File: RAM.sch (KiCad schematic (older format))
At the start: 13 parts, among them J9 RAM_CURRENT, U1 ATXMEGA128A1U-AU, U2 SN74AHC573PW, U3 IDT71V256SA

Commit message: Finished?
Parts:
- removed C28: 100n, IPC7351-Nominal:CAPC1005X55, symbol C-0402
- removed C4: 4u7, IPC7351-Nominal:CAPC1608X55, symbol C-0603
- removed J9: RAM_CURRENT, conn-100mil:CONN-100MIL-M-1x2, symbol CONN-100MIL-M-1x2
- removed R15: 0R1, IPC7351-Nominal:RESC1608X50, symbol R-0603
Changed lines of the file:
@@
 P 7100 5050
 AR Path="/56EF5511" Ref="#PWR?"  Part="1"
-AR Path="/56EF4451/56EF5511" Ref="#PWR?"  Part="1"
-F 0 "#PWR?" H 7100 5050 30  0001 C CNN
+AR Path="/56EF4451/56EF5511" Ref="#PWR21"  Part="1"
+F 0 "#PWR21" H 7100 5050 30  0001 C CNN
 F 1 "GND" H 7100 4980 30  0001 C CNN
 F 2 "" H 7100 5050 60  0000 C CNN
 F 3 "" H 7100 5050 60  0000 C CNN
 	1    7100 5050
-	1    0    0    -1
-$EndComp
-$Comp
-L C-0603 C?
-U 1 1 56EF5518
-P 7000 5700
-AR Path="/56EF5518" Ref="C?"  Part="1"
-AR Path="/56EF4451/56EF5518" Ref="C4"  Part="1"
-F 0 "C4" H 7113 5746 50  0000 L CNN
-F 1 "4u7" H 7113 5655 50  0000 L CNN
-F 2 "IPC7351-Nominal:CAPC1608X55" H 7000 5700 50  0001 C CNN
-F 3 "" H 6990 5675 60  0000 C CNN
-F 4 "CAP MLCC 4u7 10V ≥X5R 20% [0603]" H 7800 6250 60  0001 C CNN "BOM"
-	1    7000 5700
-	1    0    0    -1
-$EndComp
-$Comp
-L GND #PWR?
-U 1 1 56EF551F
-P 7000 5850
-AR Path="/56EF551F" Ref="#PWR?"  Part="1"
-AR Path="/56EF4451/56EF551F" Ref="#PWR?"  Part="1"
-F 0 "#PWR?" H 7000 5850 30  0001 C CNN
-F 1 "GND" H 7000 5780 30  0001 C CNN
-F 2 "" H 7000 5850 60  0000 C CNN
-F 3 "" H 7000 5850 60  0000 C CNN
-	1    7000 5850
-	1    0    0    -1
-$EndComp
-$Comp
-L C-0402 C?
-U 1 1 56EF5526
-P 7400 5700
-AR Path="/56EF5526" Ref="C?"  Part="1"
-AR Path="/56EF4451/56EF5526" Ref="C28"  Part="1"
-F 0 "C28" H 7513 5746 50  0000 L CNN
-F 1 "100n" H 7513 5655 50  0000 L CNN
-F 2 "IPC7351-Nominal:CAPC1005X55" H 7400 5700 50  0001 C CNN
-F 3 "" H 7390 5675 60  0000 C CNN
-F 4 "CAP MLCC 100n ≥X5R 10V 20% [0402]" H 8200 6250 60  0001 C CNN "BOM"
-	1    7400 5700
-	1    0    0    -1
-$EndComp
-$Comp
-L GND #PWR?
-U 1 1 56EF552D
-P 7400 5850
-AR Path="/56EF552D" Ref="#PWR?"  Part="1"
-AR Path="/56EF4451/56EF552D" Ref="#PWR?"  Part="1"
-F 0 "#PWR?" H 7400 5850 30  0001 C CNN
-F 1 "GND" H 7400 5780 30  0001 C CNN
-F 2 "" H 7400 5850 60  0000 C CNN
-F 3 "" H 7400 5850 60  0000 C CNN
-	1    7400 5850
 	1    0    0    -1
 $EndComp
@@
 P 5000 3000
 AR Path="/56EF553D" Ref="#PWR?"  Part="1"
-AR Path="/56EF4451/56EF553D" Ref="#PWR?"  Part="1"
-F 0 "#PWR?" H 5000 3000 30  0001 C CNN
+AR Path="/56EF4451/56EF553D" Ref="#PWR20"  Part="1"
+F 0 "#PWR20" H 5000 3000 30  0001 C CNN
 F 1 "GND" H 5000 2930 30  0001 C CNN
 F 2 "" H 5000 3000 60  0000 C CNN
@@
 	7100 5000 7050 5000
 Wire Wire Line
-	7000 5500 7000 5600
-Wire Wire Line
-	7000 5850 7000 5800
-Wire Wire Line
-	7400 4900 7400 5600
-Wire Wire Line
-	7400 5850 7400 5800
-Wire Wire Line
 	6050 3200 5750 3200
 Wire Wire Line
@@
 Wire Wire Line
 	3050 4700 3100 4700
-Wire Wire Line
-	6650 5500 7400 5500
-$Comp
-L +3.3 #PWR?
-U 1 1 56EF5658
-P 6250 5500
-AR Path="/56EF5658" Ref="#PWR?"  Part="1"
-AR Path="/56EF4451/56EF5658" Ref="#PWR?"  Part="1"
-F 0 "#PWR?" H 6250 5550 30  0001 C CNN
-F 1 "+3.3" V 6250 5588 50  0000 L CNN
-F 2 "" H 6250 5500 60  0000 C CNN
-F 3 "" H 6250 5500 60  0000 C CNN
-	1    6250 5500
-	0    -1   -1   0
-$EndComp
-$Comp
-L R-0603 R?
-U 1 1 56EF565F
-P 6550 5500
-AR Path="/56EF565F" Ref="R?"  Part="1"
-AR Path="/56EF4451/56EF565F" Ref="R15"  Part="1"
-F 0 "R15" V 6350 5500 50  0000 C CNN
-F 1 "0R1" V 6441 5500 50  0000 C CNN
-F 2 "IPC7351-Nominal:RESC1608X50" H 6550 5500 50  0001 C CNN
-F 3 "" H 6550 5550 60  0000 C CNN
-F 4 "RES SMD 0R1 1% [0603]" H 7300 6050 60  0001 C CNN "BOM"
-	1    6550 5500
-	0    1    1    0
-$EndComp
-Wire Wire Line
-	6250 5500 6450 5500
-$Comp
-L CONN-100MIL-M-1x2 J?
-U 1 1 56EF5668
-P 6600 5700
-AR Path="/56EF5668" Ref="J?"  Part="1"
-AR Path="/56EF4451/56EF5668" Ref="J9"  Part="1"
-F 0 "J9" V 6764 5647 50  0000 C CNN
-F 1 "RAM_CURRENT" V 6855 5647 50  0000 C CNN
-F 2 "conn-100mil:CONN-100MIL-M-1x2" H 6600 5700 50  0001 C CNN
-F 3 "" H 6600 5700 50  0000 C CNN
-F 4 "DIST DIGIKEY 3M9447-ND" H 6600 5700 60  0001 C CNN "BOM"
-	1    6600 5700
-	0    1    1    0
-$EndComp
-Wire Wire Line
-	6500 5650 6500 5600
-Wire Wire Line
-	6500 5600 6400 5600
-Wire Wire Line
-	6400 5600 6400 5500
-Connection ~ 6400 5500
-Wire Wire Line
-	6600 5650 6600 5600
-Wire Wire Line
-	6600 5600 6700 5600
-Wire Wire Line
-	6700 5600 6700 5500
-Connection ~ 6700 5500
-Text GLabel 6900 5200 2    50   Output ~ 0
+Text GLabel 7400 4900 2    50   Input ~ 0
 3V3RAM
-Wire Wire Line
-	6900 5200 6800 5200
-Wire Wire Line
-	6800 5200 6800 5500
-Connection ~ 6800 5500
-Connection ~ 7000 5500
-Connection ~ 7400 5500
 $Comp
 L TESTPOINT TP?
@@
 P 3700 3350
 AR Path="/56EF5685" Ref="#PWR?"  Part="1"
-AR Path="/56EF4451/56EF5685" Ref="#PWR?"  Part="1"
-F 0 "#PWR?" H 3700 3350 30  0001 C CNN
+AR Path="/56EF4451/56EF5685" Ref="#PWR19"  Part="1"
+F 0 "#PWR19" H 3700 3350 30  0001 C CNN
 F 1 "GND" H 3700 3280 30  0001 C CNN
 F 2 "" H 3700 3350 60  0000 C CNN

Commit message: Reannotate
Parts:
- renumbered R9 to R10, R23 to R11, R25 to R12, R26 to R13, R24 to R14, U2 to U4, U3 to U5
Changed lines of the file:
@@
 $EndDescr
 $Comp
-L IDT71V256SA U3
+L IDT71V256SA U5
 U 1 1 56EF54EE
 P 6550 4100
-F 0 "U3" H 6550 5267 50  0000 C CNN
+F 0 "U5" H 6550 5267 50  0000 C CNN
 F 1 "IDT71V256SA" H 6550 5176 50  0000 C CNN
 F 2 "IPC7351-Nominal:SOJ127P1118X375-28" H 6550 2900 60  0001 C CNN
@@
 P 5400 3200
 AR Path="/56EF5535" Ref="U?"  Part="1"
-AR Path="/56EF4451/56EF5535" Ref="U2"  Part="1"
-F 0 "U2" H 5400 3767 50  0000 C CNN
+AR Path="/56EF4451/56EF5535" Ref="U4"  Part="1"
+F 0 "U4" H 5400 3767 50  0000 C CNN
 F 1 "SN74AHC573PW" H 5400 3676 50  0000 C CNN
 F 2 "IPC7351-Nominal:SOP65P640X110-20" H 5400 1900 50  0001 C CNN
@@
 P 3200 1800
 AR Path="/56EF555B" Ref="R?"  Part="1"
-AR Path="/56EF4451/56EF555B" Ref="R9"  Part="1"
-F 0 "R9" V 3150 1550 50  0000 C CNN
+AR Path="/56EF4451/56EF555B" Ref="R10"  Part="1"
+F 0 "R10" V 3150 1550 50  0000 C CNN
 F 1 "68" V 3091 1800 50  0000 C CNN
 F 2 "IPC7351-Nominal:RESCAXE80P160X320X70-8" H 3200 1800 50  0001 C CNN
@@
 P 3200 1900
 AR Path="/56EF5563" Ref="R?"  Part="2"
-AR Path="/56EF4451/56EF5563" Ref="R9"  Part="2"
-F 0 "R9" V 3150 1650 50  0000 C CNN
+AR Path="/56EF4451/56EF5563" Ref="R10"  Part="2"
+F 0 "R10" V 3150 1650 50  0000 C CNN
 F 1 "68" V 3091 1900 50  0001 C CNN
 F 2 "IPC7351-Nominal:RESCAXE80P160X320X70-8" H 3200 1900 50  0001 C CNN
@@
 P 3200 2000
 AR Path="/56EF556B" Ref="R?"  Part="3"
-AR Path="/56EF4451/56EF556B" Ref="R9"  Part="3"
-F 0 "R9" V 3150 1750 50  0000 C CNN
+AR Path="/56EF4451/56EF556B" Ref="R10"  Part="3"
+F 0 "R10" V 3150 1750 50  0000 C CNN
 F 1 "68" V 3091 2000 50  0001 C CNN
 F 2 "IPC7351-Nominal:RESCAXE80P160X320X70-8" H 3200 2000 50  0001 C CNN
@@
 P 3200 2100
 AR Path="/56EF5573" Ref="R?"  Part="4"
-AR Path="/56EF4451/56EF5573" Ref="R9"  Part="4"
-F 0 "R9" V 3150 1850 50  0000 C CNN
+AR Path="/56EF4451/56EF5573" Ref="R10"  Part="4"
+F 0 "R10" V 3150 1850 50  0000 C CNN
 F 1 "68" V 3091 2100 50  0001 C CNN
 F 2 "IPC7351-Nominal:RESCAXE80P160X320X70-8" H 3200 2100 50  0001 C CNN
@@
 P 3200 2200
 AR Path="/56EF557B" Ref="R?"  Part="1"
-AR Path="/56EF4451/56EF557B" Ref="R23"  Part="1"
-F 0 "R23" V 3150 1950 50  0000 C CNN
+AR Path="/56EF4451/56EF557B" Ref="R11"  Part="1"
+F 0 "R11" V 3150 1950 50  0000 C CNN
 F 1 "68" V 3091 2200 50  0001 C CNN
 F 2 "IPC7351-Nominal:RESCAXE80P160X320X70-8" H 3200 2200 50  0001 C CNN
@@
 P 3200 2300
 AR Path="/56EF5583" Ref="R?"  Part="2"
-AR Path="/56EF4451/56EF5583" Ref="R23"  Part="2"
-F 0 "R23" V 3150 2050 50  0000 C CNN
+AR Path="/56EF4451/56EF5583" Ref="R11"  Part="2"
+F 0 "R11" V 3150 2050 50  0000 C CNN
 F 1 "68" V 3091 2300 50  0001 C CNN
 F 2 "IPC7351-Nominal:RESCAXE80P160X320X70-8" H 3200 2300 50  0001 C CNN
@@
 P 3200 2400
 AR Path="/56EF558B" Ref="R?"  Part="3"
-AR Path="/56EF4451/56EF558B" Ref="R23"  Part="3"
-F 0 "R23" V 3150 2150 50  0000 C CNN
+AR Path="/56EF4451/56EF558B" Ref="R11"  Part="3"
+F 0 "R11" V 3150 2150 50  0000 C CNN
 F 1 "68" V 3091 2400 50  0001 C CNN
 F 2 "IPC7351-Nominal:RESCAXE80P160X320X70-8" H 3200 2400 50  0001 C CNN
@@
 P 3200 2500
 AR Path="/56EF5593" Ref="R?"  Part="4"
-AR Path="/56EF4451/56EF5593" Ref="R23"  Part="4"
-F 0 "R23" V 3150 2250 50  0000 C CNN
+AR Path="/56EF4451/56EF5593" Ref="R11"  Part="4"
+F 0 "R11" V 3150 2250 50  0000 C CNN
 F 1 "68" V 3091 2500 50  0001 C CNN
 F 2 "IPC7351-Nominal:RESCAXE80P160X320X70-8" H 3200 2500 50  0001 C CNN
@@
 P 3200 5400
 AR Path="/56EF559B" Ref="R?"  Part="1"
-AR Path="/56EF4451/56EF559B" Ref="R24"  Part="1"
-F 0 "R24" V 3150 5150 50  0000 C CNN
+AR Path="/56EF4451/56EF559B" Ref="R14"  Part="1"
+F 0 "R14" V 3150 5150 50  0000 C CNN
 F 1 "68" V 3091 5400 50  0000 C CNN
 F 2 "IPC7351-Nominal:RESCAXE80P160X320X70-8" H 3200 5400 50  0001 C CNN
@@
 P 3200 5500
 AR Path="/56EF55A3" Ref="R?"  Part="2"
-AR Path="/56EF4451/56EF55A3" Ref="R24"  Part="2"
-F 0 "R24" V 3150 5250 50  0000 C CNN
+AR Path="/56EF4451/56EF55A3" Ref="R14"  Part="2"
+F 0 "R14" V 3150 5250 50  0000 C CNN
 F 1 "68" V 3091 5500 50  0001 C CNN
 F 2 "IPC7351-Nominal:RESCAXE80P160X320X70-8" H 3200 5500 50  0001 C CNN
@@
 P 3200 5600
 AR Path="/56EF55AB" Ref="R?"  Part="3"
-AR Path="/56EF4451/56EF55AB" Ref="R24"  Part="3"
-F 0 "R24" V 3150 5350 50  0000 C CNN
+AR Path="/56EF4451/56EF55AB" Ref="R14"  Part="3"
+F 0 "R14" V 3150 5350 50  0000 C CNN
 F 1 "68" V 3091 5600 50  0001 C CNN
 F 2 "IPC7351-Nominal:RESCAXE80P160X320X70-8" H 3200 5600 50  0001 C CNN
@@
 P 3200 5800
 AR Path="/56EF55B3" Ref="R?"  Part="4"
-AR Path="/56EF4451/56EF55B3" Ref="R24"  Part="4"
-F 0 "R24" V 3150 5550 50  0000 C CNN
+AR Path="/56EF4451/56EF55B3" Ref="R14"  Part="4"
+F 0 "R14" V 3150 5550 50  0000 C CNN
 F 1 "68" V 3091 5800 50  0001 C CNN
 F 2 "IPC7351-Nominal:RESCAXE80P160X320X70-8" H 3200 5800 50  0001 C CNN
@@
 P 3200 4000
 AR Path="/56EF55BB" Ref="R?"  Part="1"
-AR Path="/56EF4451/56EF55BB" Ref="R25"  Part="1"
-F 0 "R25" V 3150 3750 50  0000 C CNN
+AR Path="/56EF4451/56EF55BB" Ref="R12"  Part="1"
+F 0 "R12" V 3150 3750 50  0000 C CNN
 F 1 "68" V 3091 4000 50  0000 C CNN
 F 2 "IPC7351-Nominal:RESCAXE80P160X320X70-8" H 3200 4000 50  0001 C CNN
@@
 P 3200 4100
 AR Path="/56EF55C3" Ref="R?"  Part="2"
-AR Path="/56EF4451/56EF55C3" Ref="R25"  Part="2"
-F 0 "R25" V 3150 3850 50  0000 C CNN
+AR Path="/56EF4451/56EF55C3" Ref="R12"  Part="2"
+F 0 "R12" V 3150 3850 50  0000 C CNN
 F 1 "68" V 3091 4100 50  0001 C CNN
 F 2 "IPC7351-Nominal:RESCAXE80P160X320X70-8" H 3200 4100 50  0001 C CNN
@@
 P 3200 4200
 AR Path="/56EF55CB" Ref="R?"  Part="3"
-AR Path="/56EF4451/56EF55CB" Ref="R25"  Part="3"
-F 0 "R25" V 3150 3950 50  0000 C CNN
+AR Path="/56EF4451/56EF55CB" Ref="R12"  Part="3"
+F 0 "R12" V 3150 3950 50  0000 C CNN
 F 1 "68" V 3091 4200 50  0001 C CNN
 F 2 "IPC7351-Nominal:RESCAXE80P160X320X70-8" H 3200 4200 50  0001 C CNN
@@
 P 3200 4300
 AR Path="/56EF55D3" Ref="R?"  Part="4"
-AR Path="/56EF4451/56EF55D3" Ref="R25"  Part="4"
-F 0 "R25" V 3150 4050 50  0000 C CNN
+AR Path="/56EF4451/56EF55D3" Ref="R12"  Part="4"
+F 0 "R12" V 3150 4050 50  0000 C CNN
 F 1 "68" V 3091 4300 50  0001 C CNN
 F 2 "IPC7351-Nominal:RESCAXE80P160X320X70-8" H 3200 4300 50  0001 C CNN
@@
 P 3200 4400
 AR Path="/56EF55DB" Ref="R?"  Part="1"
-AR Path="/56EF4451/56EF55DB" Ref="R26"  Part="1"
-F 0 "R26" V 3150 4150 50  0000 C CNN
+AR Path="/56EF4451/56EF55DB" Ref="R13"  Part="1"
+F 0 "R13" V 3150 4150 50  0000 C CNN
 F 1 "68" V 3091 4400 50  0001 C CNN
 F 2 "IPC7351-Nominal:RESCAXE80P160X320X70-8" H 3200 4400 50  0001 C CNN
@@
 P 3200 4500
 AR Path="/56EF55E3" Ref="R?"  Part="2"
-AR Path="/56EF4451/56EF55E3" Ref="R26"  Part="2"
-F 0 "R26" V 3150 4250 50  0000 C CNN
+AR Path="/56EF4451/56EF55E3" Ref="R13"  Part="2"
+F 0 "R13" V 3150 4250 50  0000 C CNN
 F 1 "68" V 3091 4500 50  0001 C CNN
 F 2 "IPC7351-Nominal:RESCAXE80P160X320X70-8" H 3200 4500 50  0001 C CNN
@@
 P 3200 4600
 AR Path="/56EF55EB" Ref="R?"  Part="3"
-AR Path="/56EF4451/56EF55EB" Ref="R26"  Part="3"
-F 0 "R26" V 3150 4350 50  0000 C CNN
+AR Path="/56EF4451/56EF55EB" Ref="R13"  Part="3"
+F 0 "R13" V 3150 4350 50  0000 C CNN
 F 1 "68" V 3091 4600 50  0001 C CNN
 F 2 "IPC7351-Nominal:RESCAXE80P160X320X70-8" H 3200 4600 50  0001 C CNN
@@
 P 3200 4700
 AR Path="/56EF55F3" Ref="R?"  Part="4"
-AR Path="/56EF4451/56EF55F3" Ref="R26"  Part="4"
-F 0 "R26" V 3150 4450 50  0000 C CNN
+AR Path="/56EF4451/56EF55F3" Ref="R13"  Part="4"
+F 0 "R13" V 3150 4450 50  0000 C CNN
 F 1 "68" V 3091 4700 50  0001 C CNN
 F 2 "IPC7351-Nominal:RESCAXE80P160X320X70-8" H 3200 4700 50  0001 C CNN

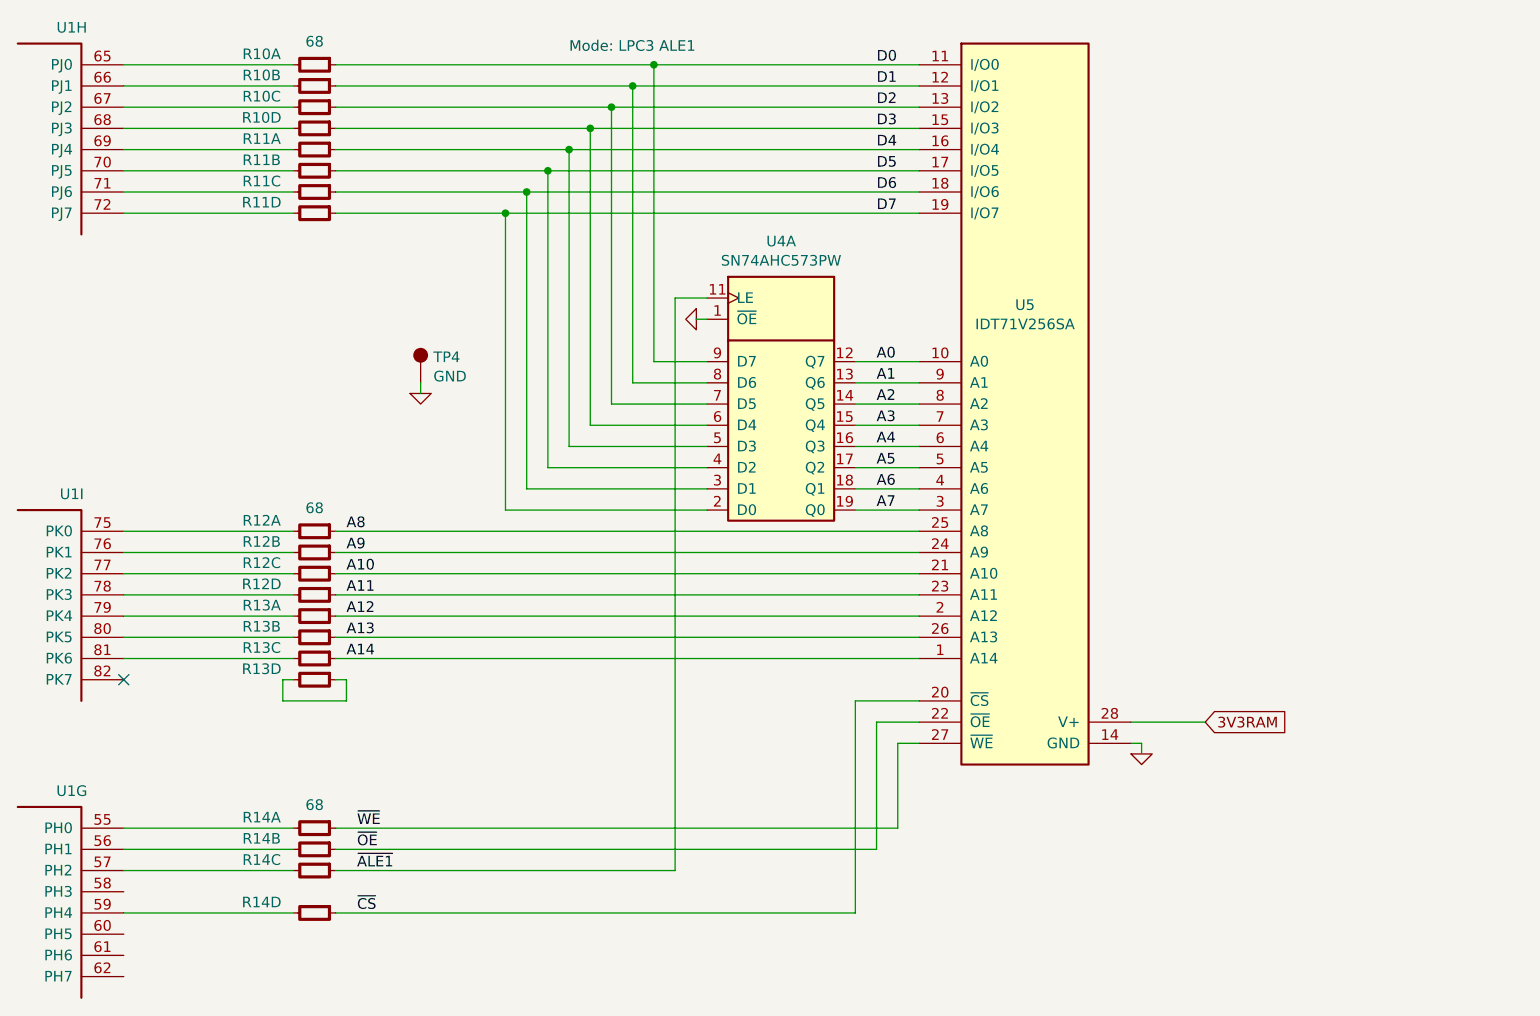
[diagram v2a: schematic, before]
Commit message: Schematic tidy-ups and add VBUS sense
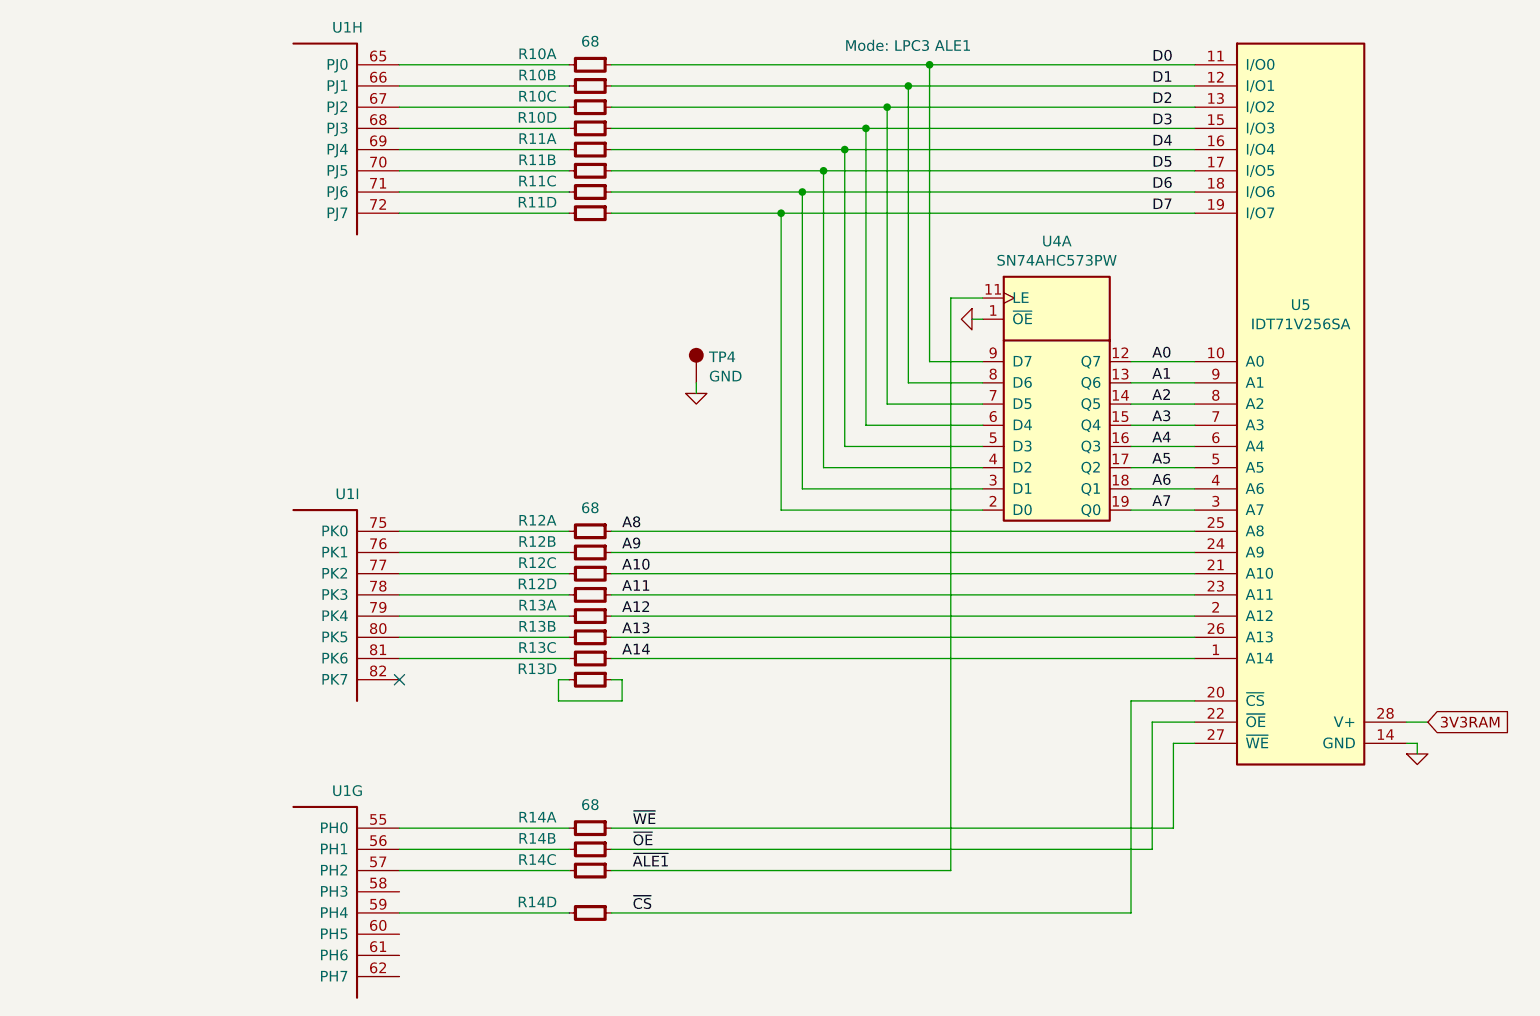
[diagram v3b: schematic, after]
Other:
- moved on the sheet: R10A, R10B, R10C, R10D, R11A, R11B, R11C, R11D, R12A, R12B, R12C, R12D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
